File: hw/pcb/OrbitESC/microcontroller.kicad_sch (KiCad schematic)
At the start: 29 parts, among them J6 CAN1, SW1 Reset, SW2 Boot, U1 TLE9250X, U11 STM32L432KBUx, U2 AT25SF081-SSHD-X, U3 24LC128

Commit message: Sync lunch schematic update
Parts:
- U11: JLCPCB (none) -> C1337280
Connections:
- net +3.3VADC: now also C11.2, C15.2
- net GND: now also C11.1, C15.1
- net SERIAL1_RST: now also U11.12 (PA6); no longer U11.2 (PC14)
- new net LED_nOE: U11.2 (PC14)
- no-connect marks 5 -> 4
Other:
- sheet Status LEDs ports: added OE; removed none
- note removed: "Missing Vdda decoupling caps"
- moved on the sheet: C11, C15, U11

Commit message: Sync PCB updates
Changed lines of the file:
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@@
   (no_connect (at 118.745 75.565))
   (no_connect (at 106.045 78.105))
-  (wire (pts (xy 99.695 102.87) (xy 102.87 102.87))
-    (stroke (width 0) (type default) (color 0 0 0 0))
-  )
   (wire (pts (xy 272.415 162.56) (xy 258.445 162.56))
     (stroke (width 0) (type default) (color 0 0 0 0))
   )
-  (wire (pts (xy 99.695 105.41) (xy 102.87 105.41))
-    (stroke (width 0) (type default) (color 0 0 0 0))
-  )
   (wire (pts (xy 127 163.195) (xy 134.62 163.195))
     (stroke (width 0) (type default) (color 0 0 0 0))
@@
     (stroke (width 0) (type default) (color 0 0 0 0))
   )
+  (wire (pts (xy 100.33 100.33) (xy 102.87 100.33))
+    (stroke (width 0) (type default) (color 0 0 0 0))
+  )
   (wire (pts (xy 304.165 99.06) (xy 304.165 96.52))
     (stroke (width 0) (type default) (color 0 0 0 0))
@@
     (stroke (width 0) (type default) (color 0 0 0 0))
   )
+  (wire (pts (xy 100.33 102.87) (xy 102.87 102.87))
+    (stroke (width 0) (type default) (color 0 0 0 0))
+  )
   (wire (pts (xy 206.375 79.375) (xy 206.375 74.295))
     (stroke (width 0) (type default) (color 0 0 0 0))
   )
-  (wire (pts (xy 99.695 100.33) (xy 102.87 100.33))
-    (stroke (width 0) (type default) (color 0 0 0 0))
-  )
   (wire (pts (xy 175.895 75.565) (xy 175.895 73.025))
     (stroke (width 0) (type default) (color 0 0 0 0))
@@
   )
   (wire (pts (xy 258.445 160.02) (xy 258.445 147.32))
+    (stroke (width 0) (type default) (color 0 0 0 0))
+  )
+  (wire (pts (xy 100.33 105.41) (xy 102.87 105.41))
     (stroke (width 0) (type default) (color 0 0 0 0))
   )
@@
   (symbol (lib_id "power:GNDD") (at 228.6 111.76 0) (unit 1)
     (in_bom yes) (on_board yes)
-    (property "Reference" "#PWR?" (id 0) (at 228.6 118.11 0)
+    (property "Reference" "#PWR024" (id 0) (at 228.6 118.11 0)
       (effects (font (size 1.27 1.27)) hide)
     )
@@
   (symbol (lib_id "power:GNDD") (at 241.3 111.76 0) (unit 1)
     (in_bom yes) (on_board yes)
-    (property "Reference" "#PWR?" (id 0) (at 241.3 118.11 0)
+    (property "Reference" "#PWR063" (id 0) (at 241.3 118.11 0)
       (effects (font (size 1.27 1.27)) hide)
     )
@@
   (symbol (lib_id "power:+3.3VADC") (at 241.3 104.14 0) (unit 1)
     (in_bom yes) (on_board yes)
-    (property "Reference" "#PWR?" (id 0) (at 245.11 105.41 0)
+    (property "Reference" "#PWR061" (id 0) (at 245.11 105.41 0)
       (effects (font (size 1.27 1.27)) hide)
     )
@@
   (symbol (lib_id "power:+3.3VADC") (at 228.6 104.14 0) (unit 1)
     (in_bom yes) (on_board yes)
-    (property "Reference" "#PWR?" (id 0) (at 232.41 105.41 0)
-      (effects (font (size 1.27 1.27)) hide)
-    )
+    (property "Reference" "#PWR023" (id 0) (at 232.41 105.41 0)
+      (effects (font (size 1.27 1.27)) hide)
+    )

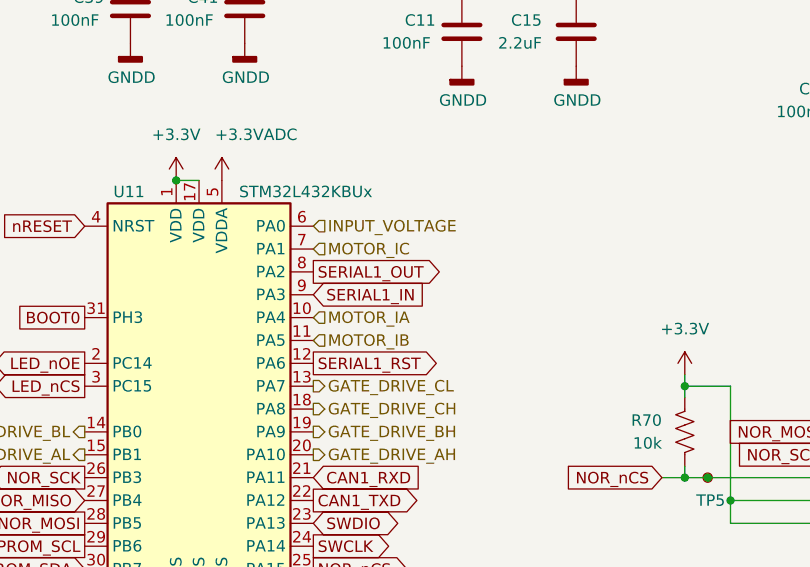
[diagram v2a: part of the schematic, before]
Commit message: Route analogs and starting power stage
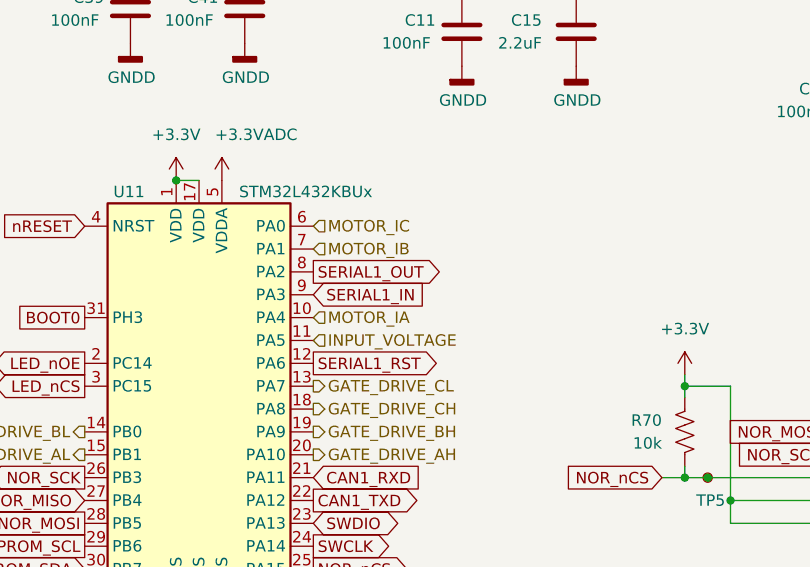
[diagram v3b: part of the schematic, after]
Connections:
- net INPUT_VOLTAGE: now also U11.11 (PA5); no longer U11.6 (PA0)
- net MOTOR_IB: now also U11.7 (PA1); no longer U11.11 (PA5)
- net MOTOR_IC: now also U11.6 (PA0); no longer U11.7 (PA1)
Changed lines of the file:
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@@
     (effects (font (size 1.27 1.27)) (justify left))
   )
-  (hierarchical_label "MOTOR_IB" (shape input) (at 212.09 142.24 0)
+  (hierarchical_label "MOTOR_IB" (shape input) (at 212.09 132.08 0)
     (effects (font (size 1.27 1.27)) (justify left))
   )
-  (hierarchical_label "INPUT_VOLTAGE" (shape input) (at 212.09 129.54 0)
+  (hierarchical_label "INPUT_VOLTAGE" (shape input) (at 212.09 142.24 0)
     (effects (font (size 1.27 1.27)) (justify left))
   )
@@
     (effects (font (size 1.27 1.27)) (justify left))
   )
-  (hierarchical_label "MOTOR_IC" (shape input) (at 212.09 132.08 0)
+  (hierarchical_label "MOTOR_IC" (shape input) (at 212.09 129.54 0)
     (effects (font (size 1.27 1.27)) (justify left))
   )

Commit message: Finalize V2 PCB
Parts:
- added TP2: NOR_MISO, TestPoint:TestPoint_Pad_D1.0mm, symbol Connector:TestPoint_Small
- C1, C11, C35, C39, C41, C52, C55: JLCPCB C307331 -> (none); LCSC (none) -> C307331
- C15: JLCPCB C49217 -> (none); LCSC (none) -> C49217
- R1, R3, R70: JLCPCB C25744 -> (none); LCSC (none) -> C25744
- R62: JLCPCB C25079 -> (none); LCSC (none) -> C25079
- R64, R77, R78: JLCPCB C25867 -> (none); LCSC (none) -> C25867
- U11: JLCPCB C1337280 -> (none); LCSC (none) -> C1337280
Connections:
- net GND: now also TP2.1
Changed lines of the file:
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@@
   (junction (at 127 150.495) (diameter 0) (color 0 0 0 0)
+  )
+  (junction (at 287.655 170.815) (diameter 0) (color 0 0 0 0)
   )
   (no_connect (at 99.06 153.035))
@@
     (stroke (width 0) (type default) (color 0 0 0 0))
   )
+  (wire (pts (xy 287.655 170.18) (xy 287.655 170.815))
+    (stroke (width 0) (type default) (color 0 0 0 0))
+  )
   (wire (pts (xy 300.355 96.52) (xy 287.655 96.52))
     (stroke (width 0) (type default) (color 0 0 0 0))
@@
   )
   (wire (pts (xy 175.895 85.725) (xy 180.975 85.725))
+    (stroke (width 0) (type default) (color 0 0 0 0))
+  )
+  (wire (pts (xy 287.655 170.815) (xy 287.655 172.085))
     (stroke (width 0) (type default) (color 0 0 0 0))
   )
@@
       (effects (font (size 1.27 1.27)) hide)
     )
-    (property "JLCPCB" "C307331" (id 4) (at 309.245 166.37 0)
+    (property "JLCPCB" "" (id 4) (at 309.245 166.37 0)
+      (effects (font (size 1.27 1.27)) hide)
+    )
+    (property "LCSC" "C307331" (id 5) (at 309.245 166.37 0)
       (effects (font (size 1.27 1.27)) hide)
     )
@@
       (effects (font (size 1.27 1.27)) hide)
     )
-    (property "JLCPCB" "C25744" (id 4) (at 206.375 83.185 0)
+    (property "JLCPCB" "" (id 4) (at 206.375 83.185 0)
+      (effects (font (size 1.27 1.27)) hide)
+    )
+    (property "LCSC" "C25744" (id 5) (at 206.375 83.185 0)
       (effects (font (size 1.27 1.27)) hide)
     )
@@
       (effects (font (size 1.27 1.27)) hide)
     )
-    (property "JLCPCB" "C25079" (id 4) (at 127 156.845 0)
+    (property "JLCPCB" "" (id 4) (at 127 156.845 0)
+      (effects (font (size 1.27 1.27)) hide)
+    )
+    (property "LCSC" "C25079" (id 5) (at 127 156.845 0)
       (effects (font (size 1.27 1.27)) hide)
     )
@@
     )
     (property "Datasheet" "" (id 3) (at 196.85 124.46 0)
+      (effects (font (size 1.27 1.27)) hide)
+    )
+    (pin "1")
+  )
+  (symbol (lib_id "Connector:TestPoint_Small") (at 287.655 170.815 0) (unit 1)
+    (in_bom yes) (on_board yes)
+    (property "Reference" "TP2" (id 0) (at 288.925 170.815 0)
+      (effects (font (size 1.27 1.27)) (justify left))
+    )
+    (property "Value" "NOR_MISO" (id 1) (at 289.56 172.0849 0)
+      (effects (font (size 1.27 1.27)) (justify left) hide)
+    )
+    (property "Footprint" "TestPoint:TestPoint_Pad_D1.0mm" (id 2) (at 292.735 170.815 0)
+      (effects (font (size 1.27 1.27)) hide)
+    )
+    (property "Datasheet" "~" (id 3) (at 292.735 170.815 0)
       (effects (font (size 1.27 1.27)) hide)
     )
@@
       (effects (font (size 1.27 1.27)) hide)
     )
-    (property "JLCPCB" "C25867" (id 4) (at 99.695 70.485 0)
+    (property "JLCPCB" "" (id 4) (at 99.695 70.485 0)
+      (effects (font (size 1.27 1.27)) hide)
+    )
+    (property "LCSC" "C25867" (id 5) (at 99.695 70.485 0)
       (effects (font (size 1.27 1.27)) hide)
     )
@@
       (effects (font (size 1.27 1.27)) hide)
     )
-    (property "JLCPCB" "C1337280" (id 4) (at 199.39 147.32 0)
+    (property "JLCPCB" "" (id 4) (at 199.39 147.32 0)
+      (effects (font (size 1.27 1.27)) hide)
+    )
+    (property "LCSC" "C1337280" (id 5) (at 199.39 147.32 0)
       (effects (font (size 1.27 1.27)) hide)
     )
@@
       (effects (font (size 1.27 1.27)) hide)
     )
-    (property "JLCPCB" "C307331" (id 4) (at 191.77 105.41 0)
+    (property "JLCPCB" "" (id 4) (at 191.77 105.41 0)
+      (effects (font (size 1.27 1.27)) hide)
+    )
+    (property "LCSC" "C307331" (id 5) (at 191.77 105.41 0)
       (effects (font (size 1.27 1.27)) hide)
     )
@@
       (effects (font (size 1.27 1.27)) hide)
     )
-    (property "JLCPCB" "C25744" (id 4) (at 253.365 152.4 0)
+    (property "JLCPCB" "" (id 4) (at 253.365 152.4 0)
+      (effects (font (size 1.27 1.27)) hide)
+    )
+    (property "LCSC" "C25744" (id 5) (at 253.365 152.4 0)
       (effects (font (size 1.27 1.27)) hide)
     )
@@
       (effects (font (size 1.27 1.27)) hide)
     )
-    (property "JLCPCB" "C25867" (id 4) (at 304.165 102.87 0)
+    (property "JLCPCB" "" (id 4) (at 304.165 102.87 0)
+      (effects (font (size 1.27 1.27)) hide)
+    )
+    (property "LCSC" "C25867" (id 5) (at 304.165 102.87 0)
       (effects (font (size 1.27 1.27)) hide)
     )
@@
       (effects (font (size 1.27 1.27)) hide)
     )
-    (property "JLCPCB" "C307331" (id 4) (at 204.47 105.41 0)
+    (property "JLCPCB" "" (id 4) (at 204.47 105.41 0)
+      (effects (font (size 1.27 1.27)) hide)
+    )
+    (property "LCSC" "C307331" (id 5) (at 204.47 105.41 0)
       (effects (font (size 1.27 1.27)) hide)
     )
@@
       (effects (font (size 1.27 1.27)) hide)
     )
-    (property "JLCPCB" "C307331" (id 4) (at 228.6 107.95 0)
+    (property "JLCPCB" "" (id 4) (at 228.6 107.95 0)
+      (effects (font (size 1.27 1.27)) hide)
+    )
+    (property "LCSC" "C307331" (id 5) (at 228.6 107.95 0)
       (effects (font (size 1.27 1.27)) hide)
     )
@@
       (effects (font (size 1.27 1.27)) hide)
     )
-    (property "JLCPCB" "C25744" (id 4) (at 180.975 67.945 0)
+    (property "JLCPCB" "" (id 4) (at 180.975 67.945 0)
+      (effects (font (size 1.27 1.27)) hide)
+    )
+    (property "LCSC" "C25744" (id 5) (at 180.975 67.945 0)
       (effects (font (size 1.27 1.27)) hide)
     )
@@
       (effects (font (size 1.27 1.27)) hide)
     )
-    (property "JLCPCB" "C49217" (id 4) (at 241.3 107.95 0)
+    (property "JLCPCB" "" (id 4) (at 241.3 107.95 0)
+      (effects (font (size 1.27 1.27)) hide)
+    )
+    (property "LCSC" "C49217" (id 5) (at 241.3 107.95 0)
       (effects (font (size 1.27 1.27)) hide)
     )
@@
       (effects (font (size 1.27 1.27)) hide)
     )
-    (property "JLCPCB" "C307331" (id 4) (at 175.895 79.375 0)
+    (property "JLCPCB" "" (id 4) (at 175.895 79.375 0)
+      (effects (font (size 1.27 1.27)) hide)
+    )
+    (property "LCSC" "C307331" (id 5) (at 175.895 79.375 0)
       (effects (font (size 1.27 1.27)) hide)
     )
@@
       (effects (font (size 1.27 1.27)) hide)
     )
-    (property "JLCPCB" "C307331" (id 4) (at 272.415 115.57 0)
+    (property "JLCPCB" "" (id 4) (at 272.415 115.57 0)
+      (effects (font (size 1.27 1.27)) hide)
+    )
+    (property "LCSC" "C307331" (id 5) (at 272.415 115.57 0)
       (effects (font (size 1.27 1.27)) hide)
     )
@@
       (effects (font (size 1.27 1.27)) hide)
     )
-    (property "JLCPCB" "C307331" (id 4) (at 81.28 154.305 0)
+    (property "JLCPCB" "" (id 4) (at 81.28 154.305 0)
+      (effects (font (size 1.27 1.27)) hide)
+    )
+    (property "LCSC" "C307331" (id 5) (at 81.28 154.305 0)
       (effects (font (size 1.27 1.27)) hide)
     )
@@
     (pin "1")
   )
-  (symbol (lib_id "power:GNDD") (at 287.655 170.18 0) (unit 1)
-    (in_bom yes) (on_board yes)
-    (property "Reference" "#PWR0115" (id 0) (at 287.655 176.53 0)
-      (effects (font (size 1.27 1.27)) hide)
-    )
-    (property "Value" "GNDD" (id 1) (at 285.115 173.99 0)
-      (effects (font (size 1.27 1.27)) (justify left))
-    )
-    (property "Footprint" "" (id 2) (at 287.655 170.18 0)
-      (effects (font (size 1.27 1.27)) hide)
-    )
-    (property "Datasheet" "" (id 3) (at 287.655 170.18 0)
+  (symbol (lib_id "power:GNDD") (at 287.655 172.085 0) (unit 1)
+    (in_bom yes) (on_board yes)
+    (property "Reference" "#PWR0115" (id 0) (at 287.655 178.435 0)
+      (effects (font (size 1.27 1.27)) hide)
+    )
+    (property "Value" "GNDD" (id 1) (at 285.115 175.895 0)
+      (effects (font (size 1.27 1.27)) (justify left))
+    )
+    (property "Footprint" "" (id 2) (at 287.655 172.085 0)
+      (effects (font (size 1.27 1.27)) hide)
+    )
+    (property "Datasheet" "" (id 3) (at 287.655 172.085 0)
       (effects (font (size 1.27 1.27)) hide)
     )
@@
       (effects (font (size 1.27 1.27)) hide)
     )
-    (property "JLCPCB" "C25867" (id 4) (at 300.355 102.87 0)
-      (effects (font (size 1.27 1.27)) hide)
-    )
+    (property "JLCPCB" "" (id 4) (at 300.355 102.87 0)
+      (effects (font (size 1.27 1.27)) hide)
+    )
+    (property "LCSC" "C25867" (id 5) (at 300.355 102.87 0)
+      (effects (font (size 1.27 1.27)) hide)
+    )

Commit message: Sync work
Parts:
- U11: value STM32L432KBUx -> STM32L432KCU6
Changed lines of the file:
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@@
       (effects (font (size 1.27 1.27)) (justify left))
     )
-    (property "Value" "STM32L432KBUx" (id 1) (at 203.835 125.73 0)
+    (property "Value" "STM32L432KCU6" (id 1) (at 203.835 125.73 0)
       (effects (font (size 1.27 1.27)) (justify left))
     )
